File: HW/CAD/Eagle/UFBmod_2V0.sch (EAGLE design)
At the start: 161 parts, among them T0551 MMBT2222, U0501 MIDAS_MCCOG21605B6W-FPTLWI, U0601 MAX5217, U0701 AT86RF215-ZU, U0711 ASVTX-13-D-26.000MHZ-I05-T, U0811 PE4259, U0821 RFX1010, U0881 B39871B3440U410, U0911 FT232HL, U1101 TPS53353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

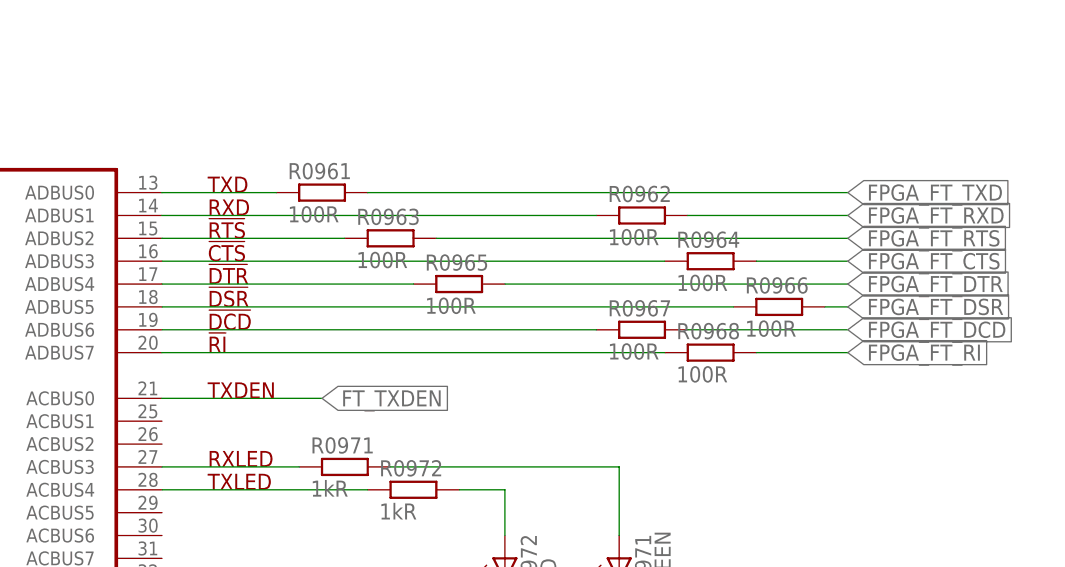
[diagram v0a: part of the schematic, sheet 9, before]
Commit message: HW_2V0 - HW/CAD/Eagle - all parts placed for the first time
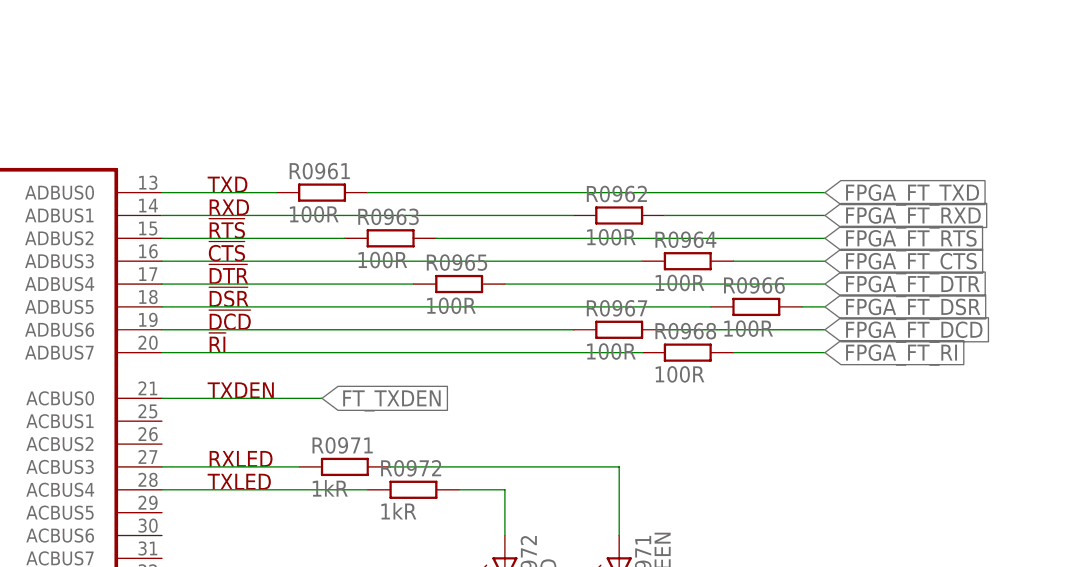
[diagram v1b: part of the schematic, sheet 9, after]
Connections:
- net FPGA_FT_12MHZ: now also JB2.B15_IO25
- net FPGA_FT_CTS: now also JB2.B15_L21_N
- net FPGA_FT_DCD: now also JB2.B15_L22_N
- net FPGA_FT_DSR: now also JB2.B15_L24_P
- net FPGA_FT_DTR: now also JB2.B15_L24_N
- net FPGA_FT_RESET: now also JB2.B15_L15_N
- net FPGA_FT_RI: now also JB2.B15_L22_P
- net FPGA_FT_RTS: now also JB2.B15_L21_P
- net FPGA_FT_RXD: now also JB2.B15_L6_P
- net FPGA_FT_TXD: now also JB2.B15_L6_N
- net FPGA_RFX_MODE: now also JB2.B15_L15_P
- net RFX_TXEN: now also U0811.CTRL
- net TRX_FEA09: no longer U0811.CTRL
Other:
- moved on the sheet: R0962, R0964, R0966, R0967, R0968

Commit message: HW_2V0 - HW/CAD/Eagle - work of the day
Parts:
- removed X1321, X1322, X1323: PHOENIX_1990067_1X8X2MM50_PTSA-0-5, df4iah_connector:PHOENIX_1990067_1X8X2MM50_PTSA-0-5
- added C1350: 100nF, df4iah_rcl:C-EUC0402
- added R1351, R1352, R1353, R1354, R1355, R1356, R1357, R1358, R1361, R1362, R1363, R1364, R1365, R1366, R1367, R1368, R1371, R1372, R1373, R1374, R1375, R1376: 100R, df4iah_rcl:R-EU_R0402
- added X1350: (no value), df4iah_connector:HEADER-2X3
- added X1351, X1361, X1371: PHOENIX_1990067_1X8X2MM50_PTSA-0-5, df4iah_connector:PHOENIX_1990067_1X8X2MM50_PTSA-0-5
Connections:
- new net B2W_51: R1351.2, X1351.1
- new net B2W_52: R1352.2, X1351.2
- new net B2W_53: R1353.2, X1351.3
- new net B2W_54: R1354.2, X1351.4
- new net B2W_55: R1355.2, X1351.5
- new net B2W_56: R1356.2, X1351.6
- new net B2W_57: R1357.2, X1351.7
- new net B2W_58: R1358.2, X1351.8
- new net B2W_61: R1361.2, X1361.1
- new net B2W_62: R1362.2, X1361.2
- new net B2W_63: R1363.2, X1361.3
- new net B2W_64: R1364.2, X1361.4
- new net B2W_65: R1365.2, X1361.5
- new net B2W_66: R1366.2, X1361.6
- new net B2W_67: R1367.2, X1361.7
- new net B2W_68: R1368.2, X1361.8
- new net B2W_71: R1371.2, X1371.1
- new net B2W_72: R1372.2, X1371.2
- new net B2W_73: R1373.2, X1371.3
- new net B2W_74: R1374.2, X1371.4
- new net B2W_75: R1375.2, X1371.5
- new net B2W_76: R1376.2, X1371.6
- new net FPGA_B16_L10_N: JB1.B16_L10_N, R1368.1
- new net FPGA_B16_L10_P: JB1.B16_L10_P, R1367.1
- new net FPGA_B16_L11_N: JB1.B16_L11_N, R1366.1
- new net FPGA_B16_L11_P: JB1.B16_L11_P, R1365.1
- new net FPGA_B16_L16_N: JB1.B16_L16_N, R1352.1
- new net FPGA_B16_L16_P: JB1.B16_L16_P, R1351.1
- new net FPGA_B16_L17_N: JB1.B16_L17_N, R1356.1
- new net FPGA_B16_L17_P: JB1.B16_L17_P, R1355.1
- new net FPGA_B16_L18_N: JB1.B16_L18_N, R1358.1
- new net FPGA_B16_L18_P: JB1.B16_L18_P, R1357.1
- new net FPGA_B16_L19_N: JB1.B16_L19_N, R1354.1
- new net FPGA_B16_L19_P: JB1.B16_L19_P, R1353.1
- new net FPGA_B16_L2_N: JB1.B16_L2_N, R1374.1
- new net FPGA_B16_L2_P: JB1.B16_L2_P, R1373.1
- new net FPGA_B16_L5_N: JB1.B16_L5_N, R1372.1
- new net FPGA_B16_L5_P: JB1.B16_L5_P, R1371.1
- new net FPGA_B16_L6_N: JB1.B16_L6_N, R1376.1
- new net FPGA_B16_L6_P: JB1.B16_L6_P, R1375.1
- new net FPGA_B16_L7_N: JB1.B16_L7_N, R1364.1
- new net FPGA_B16_L7_P: JB1.B16_L7_P, R1363.1
- new net FPGA_B16_L9_N: JB1.B16_L9_N, R1362.1
- new net FPGA_B16_L9_P: JB1.B16_L9_P, R1361.1
- new net VCCIO16: C1350.2, JB1.VCCIO16@10, JB1.VCCIO16@12, X1350.1, X1350.3, X1350.5
- net +2V5: now also X1350.4
- net GND: now also C1350.1, X1371.8; no longer X1323.8
- net U1V8: now also X1350.2
- net U3V3: now also X1350.6; no longer JB1.VCCIO16@10, JB1.VCCIO16@12
- net VIN_PWR: now also X1371.7; no longer X1323.7
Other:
- moved on the sheet: R1331, R1332, R1333, R1334, R1335, R1337, R1338, R1339, X1331, X1332

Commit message: HW_2V0 - HW/CAD/Eagle - ARJE-0034 added
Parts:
- removed H1411, H1412, H1413, H1414: MOUNT-PAD-ROUND3.2, df4iah_holes:MOUNT-PAD-ROUND3.2
- added C1431, C1441: 1uF, df4iah_rcl:C-EUC0402
- added C1432, C1442: 100nF, df4iah_rcl:C-EUC0402
- added H1511, H1512, H1513, H1514: MOUNT-PAD-ROUND3.2, df4iah_holes:MOUNT-PAD-ROUND3.2
- added J1411: (no value), df4iah_connector:ARJE-0034_RJ45_WITH_MAGNETICS
- added R1421, R1422: 1kR, df4iah_rcl:R-EU_R0402
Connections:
- new net ETH_DA_G: J1411.12, R1422.2
- new net ETH_DA_Y: J1411.1, R1421.2
- new net FPGA_ETH_DA_G: R1422.1
- new net FPGA_ETH_DA_Y: R1421.1
- net +3V3: now also C1431.1, C1432.1, C1441.1, C1442.1, J1411.5, J1411.6
- net FPGA_ETH_RD_N: now also J1411.8
- net FPGA_ETH_RD_P: now also J1411.7
- net FPGA_ETH_TD_N: now also J1411.4
- net FPGA_ETH_TD_P: now also J1411.3
- net GND: now also C1431.2, C1432.2, C1441.2, C1442.2, H1511.MOUNT, H1512.MOUNT, H1513.MOUNT, H1514.MOUNT, J1411.10, J1411.11, J1411.13, J1411.2; no longer H1411.MOUNT, H1412.MOUNT, H1413.MOUNT, H1414.MOUNT
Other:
- note added: "Connectors 1"
- note added: "Connectors 2"
- note added: "Ethernet 100MBit Connector"
- note added: "RX+"
- note added: "RX-"
- note added: "TX+"
- note added: "TX-"
- note removed: "Connectors"

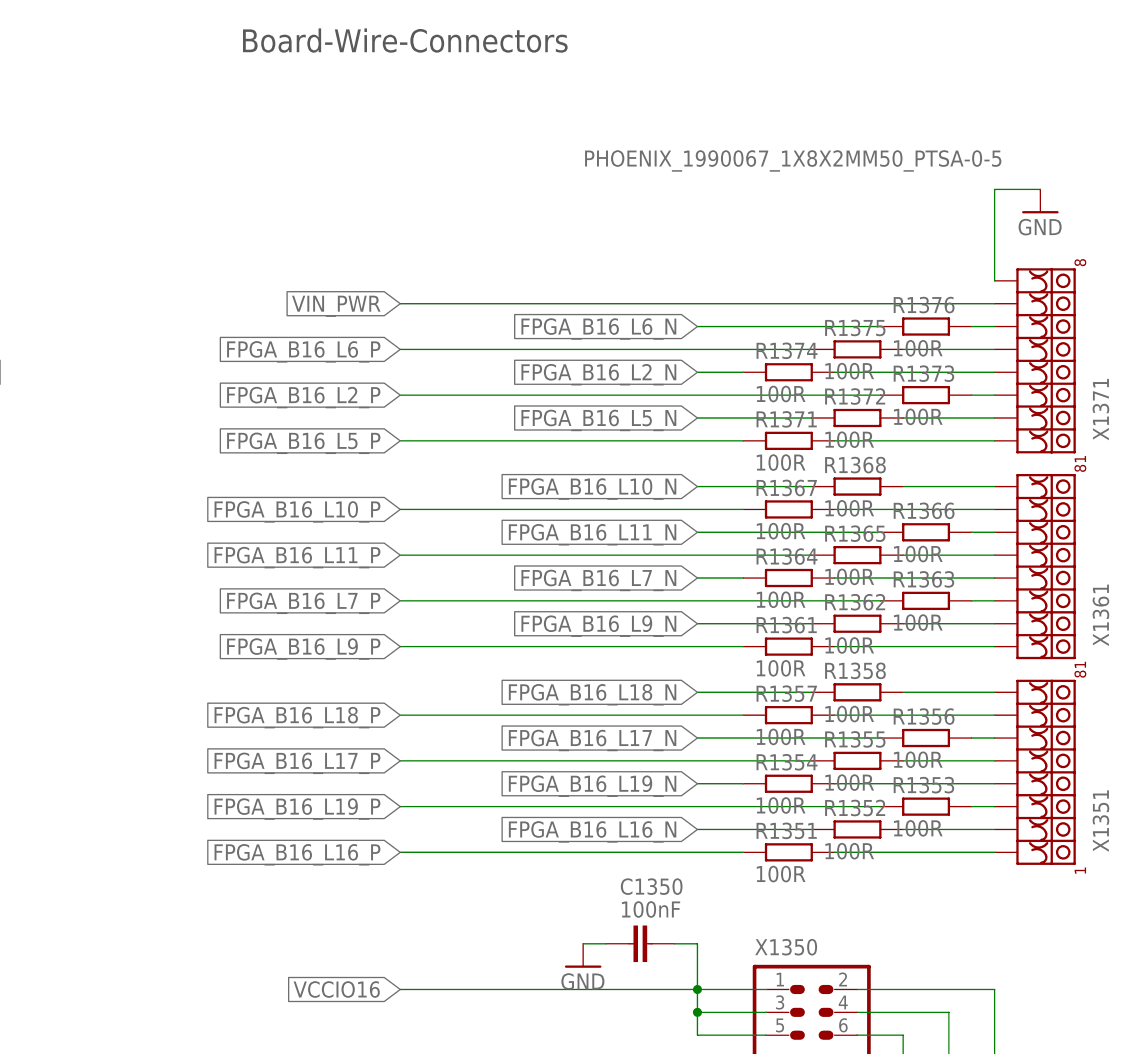
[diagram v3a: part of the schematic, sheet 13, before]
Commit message: HW_2V0 - HW/CAD/Eagle - ARJE-0034 placed
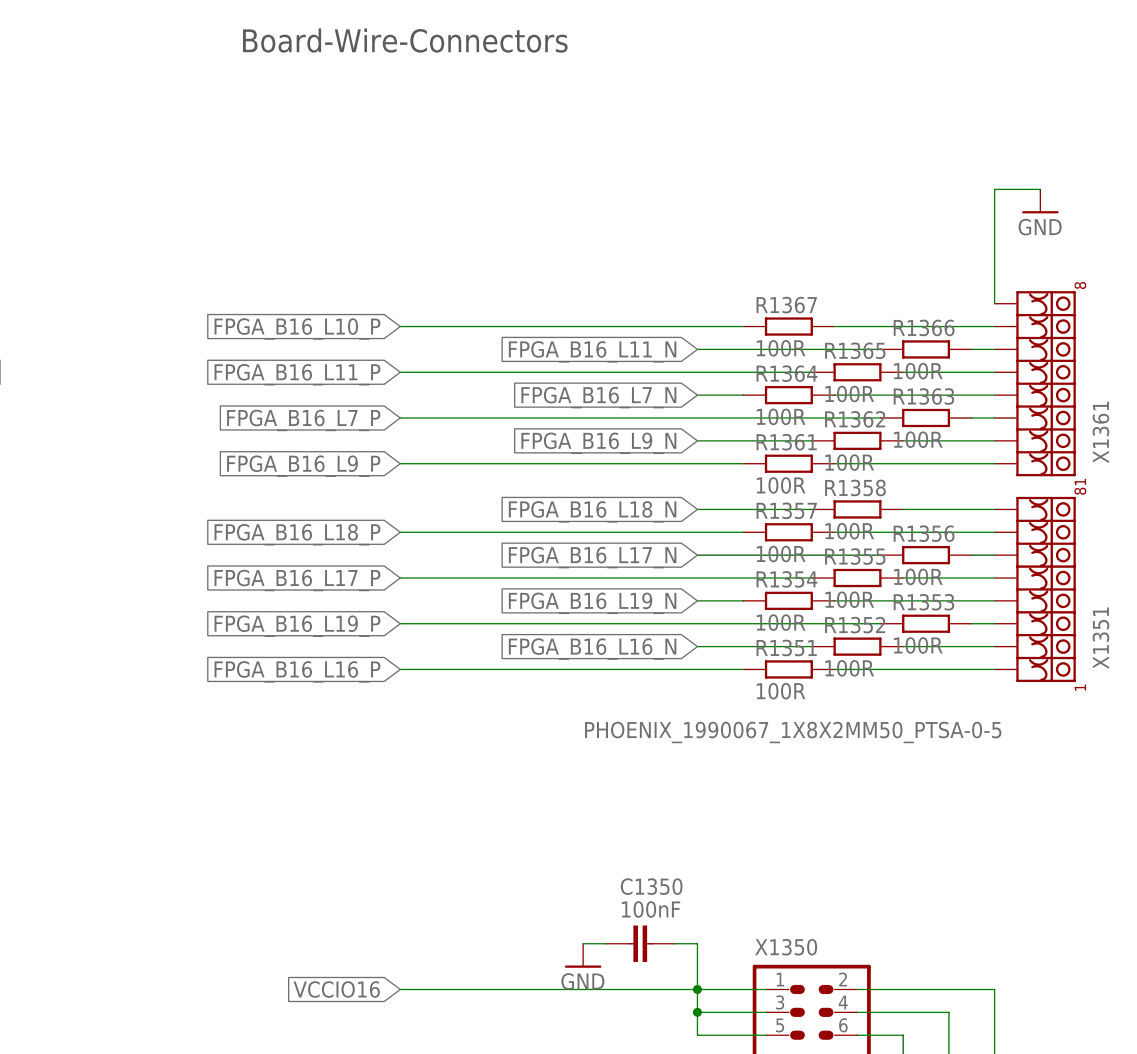
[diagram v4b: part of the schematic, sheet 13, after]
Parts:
- removed R1368, R1371, R1372, R1373, R1374, R1375, R1376: 100R, df4iah_rcl:R-EU_R0402
- removed X1371: PHOENIX_1990067_1X8X2MM50_PTSA-0-5, df4iah_connector:PHOENIX_1990067_1X8X2MM50_PTSA-0-5
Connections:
- removed net B2W_68: R1368.2, X1361.8
- removed net B2W_71: R1371.2, X1371.1
- removed net B2W_72: R1372.2, X1371.2
- removed net B2W_73: R1373.2, X1371.3
- removed net B2W_74: R1374.2, X1371.4
- removed net B2W_75: R1375.2, X1371.5
- removed net B2W_76: R1376.2, X1371.6
- net FPGA_B16_L10_N: no longer R1368.1
- net FPGA_B16_L2_N: no longer R1374.1
- net FPGA_B16_L2_P: no longer R1373.1
- net FPGA_B16_L5_N: no longer R1372.1
- net FPGA_B16_L5_P: no longer R1371.1
- net FPGA_B16_L6_N: no longer R1376.1
- net FPGA_B16_L6_P: no longer R1375.1
- net GND: now also X1361.8; no longer X1371.8
- net VIN_PWR: no longer X1371.7
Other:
- moved on the sheet: R1351, R1352, R1353, R1354, R1355, R1356, R1357, R1358, R1361, R1362, R1363, R1364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
